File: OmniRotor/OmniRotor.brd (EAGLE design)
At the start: 50 x 50 mm, 160 parts, among them CON1 Telem, CON2 SPI, CON3 Utility, CON4 I2C, CON5 I2C, CON6 ADC, CON7 RC_IN, CON8 SWD, CON9 GPS, Q1 16MHz, U1 MS5611-B03, U10 LP2985-3.3 (MCP1801T-3302I), U2 LPS331AP, U4 HMC5883L, U5 BMP180, U6 STM32F405RG, U7 XOR, U8 LP2985-3.3 (MCP1802T-3302I), U9 LP2985-3.3 (MCP1801T-3302I)

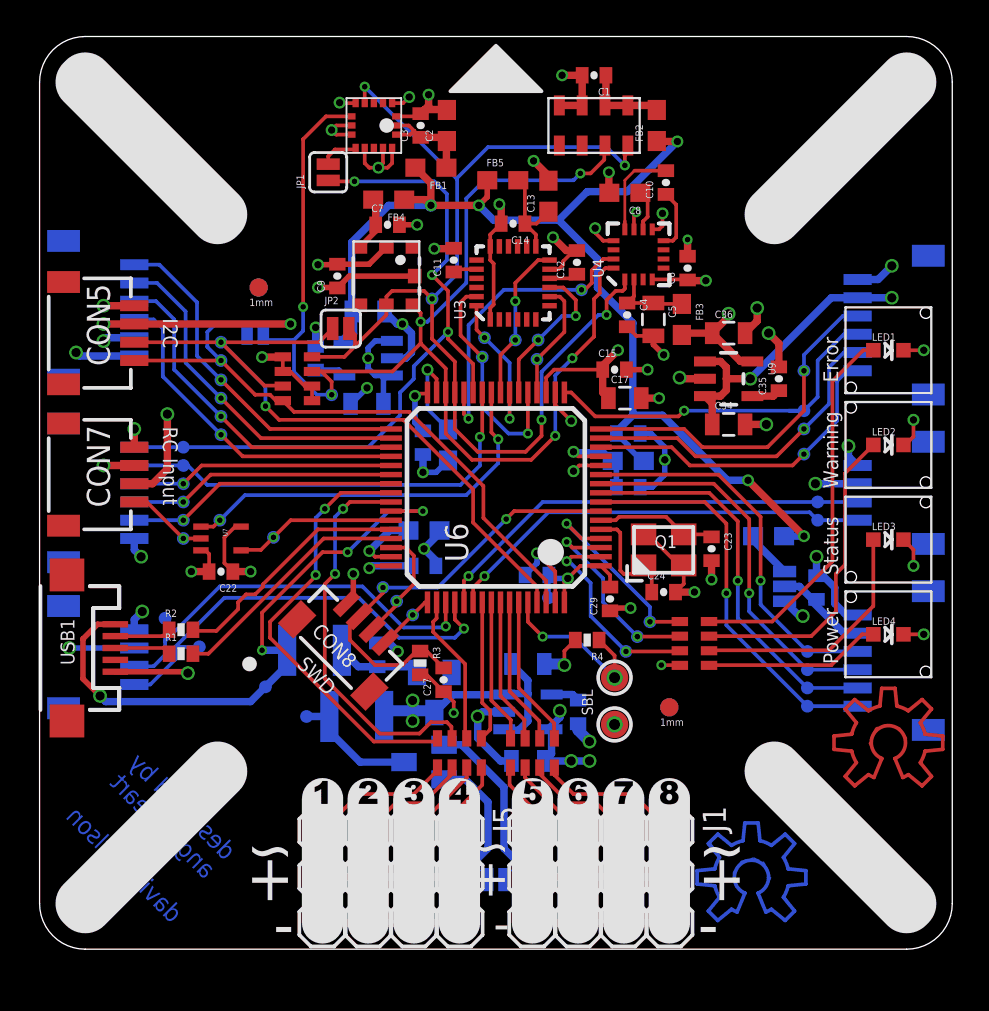
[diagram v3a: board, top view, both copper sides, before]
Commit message: Silkscreen and component footprint updates
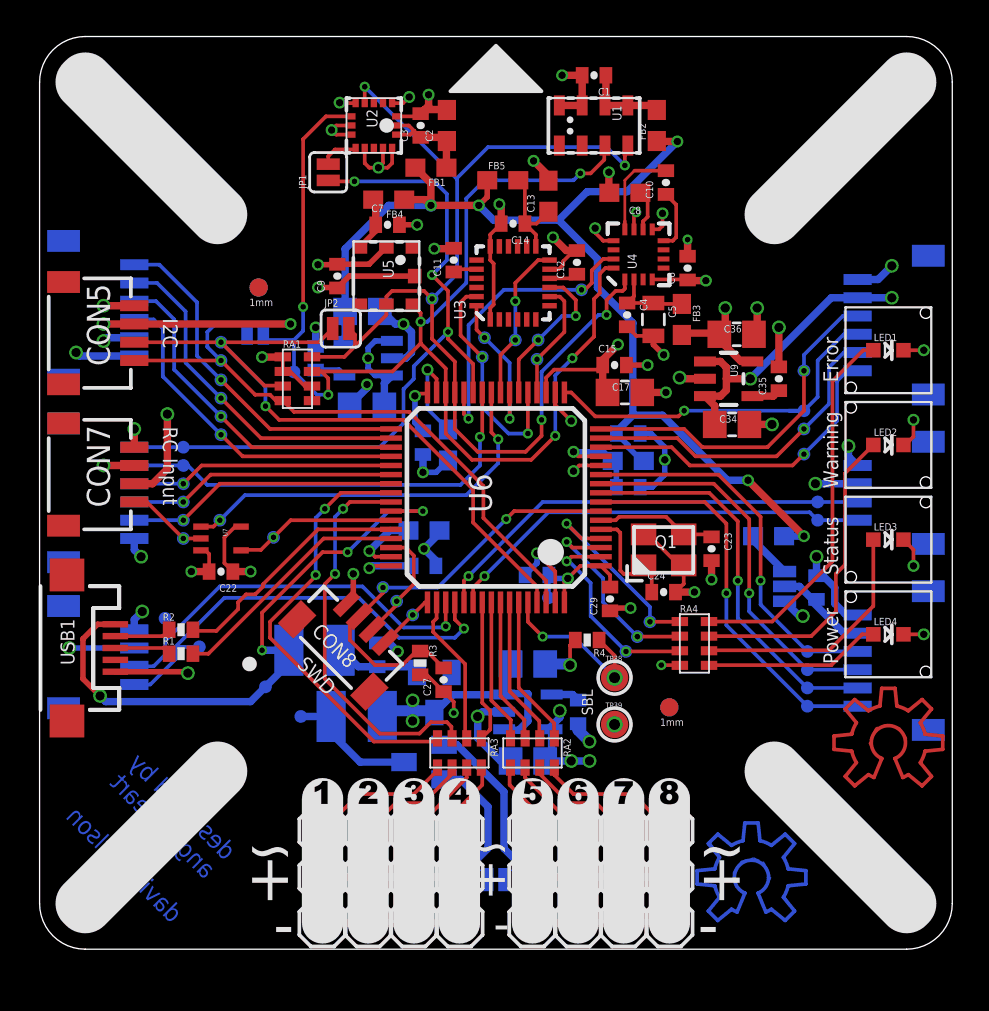
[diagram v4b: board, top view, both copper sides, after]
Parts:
- C1, C10, C11, C12, C14, C15, C18, C19, C20, C21, C22, C23, C24, C26, C27, C28, C29, C3, C30, C32, C35, C38, C4, C6, C7, C9: device OmniLoco:0402-CAP -> OmniLoco:0402-CAP@1
- C13, C16, C2, C25, C8: device OmniLoco:0603 -> OmniLoco:0603@1
- C5: device OmniLoco:0805 -> OmniLoco:0805@1
- moved TP6 2.41 mm to (13.9, 31.6)
- moved C36 0.44 mm to (38.2, 33.7)
- moved TP44 0.36 mm to (37.6, 35.1)
- moved C17 0.31 mm to (32.1, 30.5)
- moved C39 0.31 mm to (17.7, 34.9)
- moved TP42 0.31 mm to (14.3, 12.8)
- moved C15 0.25 mm to (31.5, 32.0)
- moved C34 0.19 mm to (37.9, 28.8)
- moved C37 0.12 mm to (17.9, 29.8)
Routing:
- net GND: track 152.2 -> 153.2 mm
